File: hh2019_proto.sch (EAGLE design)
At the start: 145 parts, among them IC1 CP210X_USB_UART, IC2 AP2114H, IC4 TP4056, J1 PJ-313D, Q1 MMBT2222A, Q3 MMBT2222A, Q4 MMBT2222A, Q5 SI1304 BDL, T1 MOSFET-PCHANNEL, T2 MOSFET-PCHANNEL, U1 MPR121QR2, U2 ESP32-WROVER-I, U3 PCM5102A, X4 JST-PH3

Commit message: All but the last handful passives placed and routed
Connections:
- net N$8 renamed RST
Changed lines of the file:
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@@
 </segment>
 </net>
-<net name="N$8" class="0">
+<net name="RST" class="0">
 <segment>
 <pinref part="IC1" gate="G$1" pin="!RST"/>

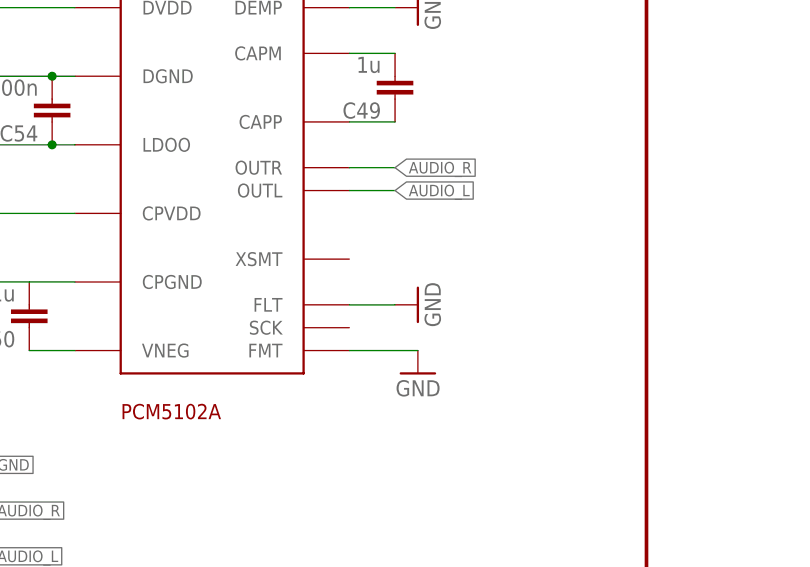
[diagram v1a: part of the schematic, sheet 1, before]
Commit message: Added missing DAC connections. Fixes #1
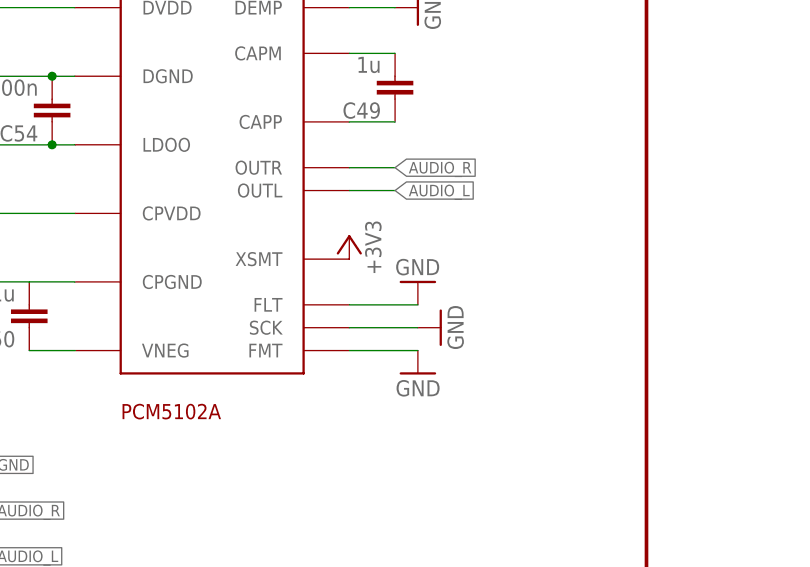
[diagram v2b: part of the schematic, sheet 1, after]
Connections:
- new net +3V3: U3.XSMT
- net GND: now also U3.SCK
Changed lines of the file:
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@@
 <part name="GND18" library="supply1" deviceset="GND" device=""/>
 <part name="GND55" library="supply1" deviceset="GND" device=""/>
+<part name="GND56" library="supply1" deviceset="GND" device=""/>
+<part name="+2V7" library="supply1" deviceset="+3V3" device=""/>
 </parts>
 <sheets>
@@
 <attribute name="VALUE" x="205.74" y="116.84" size="1.778" layer="96" rot="MR270"/>
 </instance>
-<instance part="GND3" gate="1" x="203.2" y="81.28" smashed="yes" rot="MR270">
-<attribute name="VALUE" x="205.74" y="83.82" size="1.778" layer="96" rot="MR270"/>
+<instance part="GND3" gate="1" x="203.2" y="83.82" smashed="yes" rot="MR180">
+<attribute name="VALUE" x="200.66" y="86.36" size="1.778" layer="96" rot="MR180"/>
 </instance>
 <instance part="GND17" gate="1" x="203.2" y="73.66" smashed="yes" rot="MR0">
@@
 <instance part="GND55" gate="1" x="144.78" y="104.14" smashed="yes" rot="MR0">
 <attribute name="VALUE" x="147.32" y="101.6" size="1.778" layer="96" rot="MR0"/>
+</instance>
+<instance part="GND56" gate="1" x="205.74" y="78.74" smashed="yes" rot="MR270">
+<attribute name="VALUE" x="208.28" y="81.28" size="1.778" layer="96" rot="MR270"/>
+</instance>
+<instance part="+2V7" gate="G$1" x="195.58" y="88.9" smashed="yes">
+<attribute name="VALUE" x="199.136" y="84.582" size="1.778" layer="96" rot="R90"/>
 </instance>
 </instances>
@@
 <segment>
 <pinref part="U3" gate="G$1" pin="FLT"/>
-<wire x1="195.58" y1="81.28" x2="200.66" y2="81.28" width="0.1524" layer="91"/>
+<wire x1="195.58" y1="81.28" x2="203.2" y2="81.28" width="0.1524" layer="91"/>
 <pinref part="GND3" gate="1" pin="GND"/>
 </segment>
@@
 <pinref part="C54" gate="G$1" pin="2"/>
 <pinref part="GND55" gate="1" pin="GND"/>
+</segment>
+<segment>
+<pinref part="U3" gate="G$1" pin="SCK"/>
+<pinref part="GND56" gate="1" pin="GND"/>
+<wire x1="203.2" y1="78.74" x2="195.58" y2="78.74" width="0.1524" layer="91"/>
 </segment>
 </net>
@@
 </segment>
 </net>
+<net name="+3V3" class="0">
+<segment>
+<pinref part="U3" gate="G$1" pin="XSMT"/>
+<pinref part="+2V7" gate="G$1" pin="+3V3"/>
+</segment>
+</net>

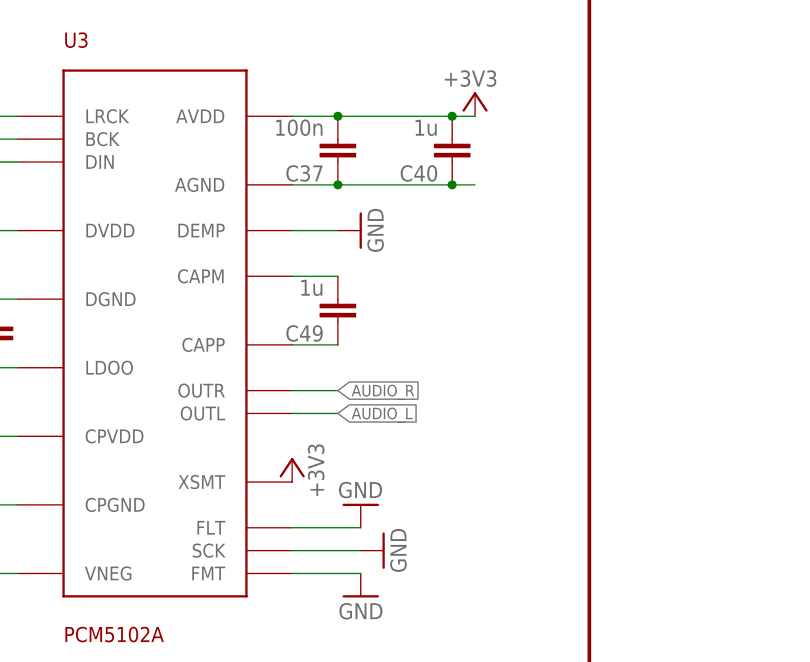
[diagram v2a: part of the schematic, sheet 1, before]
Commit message: Fixed floating DAC pins being unconnected
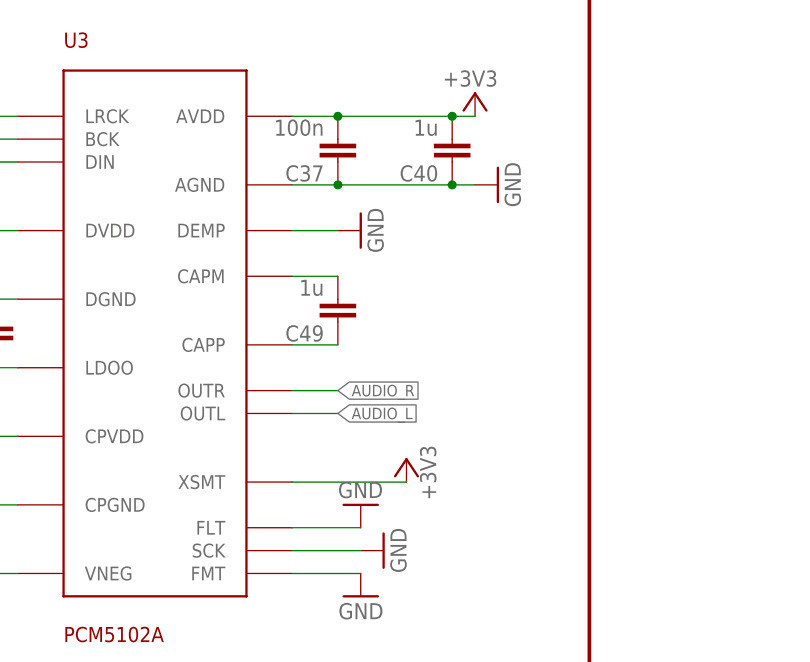
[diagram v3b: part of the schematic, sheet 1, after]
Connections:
- removed net +3V3: U3.XSMT
- removed net DEMP: U3.DEMP
- net 3V3: now also U3.XSMT
- net GND: now also U3.DEMP
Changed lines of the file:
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@@
 <part name="GND18" library="supply1" deviceset="GND" device=""/>
 <part name="GND55" library="supply1" deviceset="GND" device=""/>
+<part name="GND" library="supply1" deviceset="GND" device=""/>
 <part name="GND56" library="supply1" deviceset="GND" device=""/>
 <part name="+2V7" library="supply1" deviceset="+3V3" device=""/>
@@
 <attribute name="VALUE" x="147.32" y="101.6" size="1.778" layer="96" rot="MR0"/>
 </instance>
-<instance part="GND56" gate="1" x="205.74" y="78.74" smashed="yes" rot="MR270">
+<instance part="GND" gate="1" x="205.74" y="78.74" smashed="yes" rot="MR270">
 <attribute name="VALUE" x="208.28" y="81.28" size="1.778" layer="96" rot="MR270"/>
 </instance>
-<instance part="+2V7" gate="G$1" x="195.58" y="88.9" smashed="yes">
-<attribute name="VALUE" x="199.136" y="84.582" size="1.778" layer="96" rot="R90"/>
+<instance part="GND56" gate="1" x="218.44" y="119.38" smashed="yes" rot="MR270">
+<attribute name="VALUE" x="220.98" y="121.92" size="1.778" layer="96" rot="MR270"/>
+</instance>
+<instance part="+2V7" gate="G$1" x="208.28" y="88.9" smashed="yes">
+<attribute name="VALUE" x="211.582" y="84.328" size="1.778" layer="96" rot="R90"/>
 </instance>
 </instances>
@@
 <pinref part="C40" gate="G$1" pin="1"/>
 <junction x="213.36" y="119.38"/>
+<pinref part="GND56" gate="1" pin="GND"/>
 </segment>
 <segment>
@@
 <segment>
 <pinref part="U3" gate="G$1" pin="SCK"/>
-<pinref part="GND56" gate="1" pin="GND"/>
+<pinref part="GND" gate="1" pin="GND"/>
 <wire x1="203.2" y1="78.74" x2="195.58" y2="78.74" width="0.1524" layer="91"/>
+</segment>
+<segment>
+<pinref part="U3" gate="G$1" pin="DEMP"/>
+<wire x1="195.58" y1="114.3" x2="200.66" y2="114.3" width="0.1524" layer="91"/>
+<pinref part="GND2" gate="1" pin="GND"/>
 </segment>
 </net>
@@
 <pinref part="+2V6" gate="G$1" pin="+3V3"/>
 </segment>
+<segment>
+<pinref part="U3" gate="G$1" pin="XSMT"/>
+<pinref part="+2V7" gate="G$1" pin="+3V3"/>
+<wire x1="195.58" y1="86.36" x2="208.28" y2="86.36" width="0.1524" layer="91"/>
+</segment>
 </net>
 <net name="GDR" class="0">
@@
 </segment>
 </net>
-<net name="DEMP" class="2">
-<segment>
-<pinref part="U3" gate="G$1" pin="DEMP"/>
-<wire x1="195.58" y1="114.3" x2="200.66" y2="114.3" width="0.1524" layer="91"/>
-<pinref part="GND2" gate="1" pin="GND"/>
-</segment>
-</net>
-<net name="+3V3" class="0">
-<segment>
-<pinref part="U3" gate="G$1" pin="XSMT"/>
-<pinref part="+2V7" gate="G$1" pin="+3V3"/>
-</segment>
-</net>

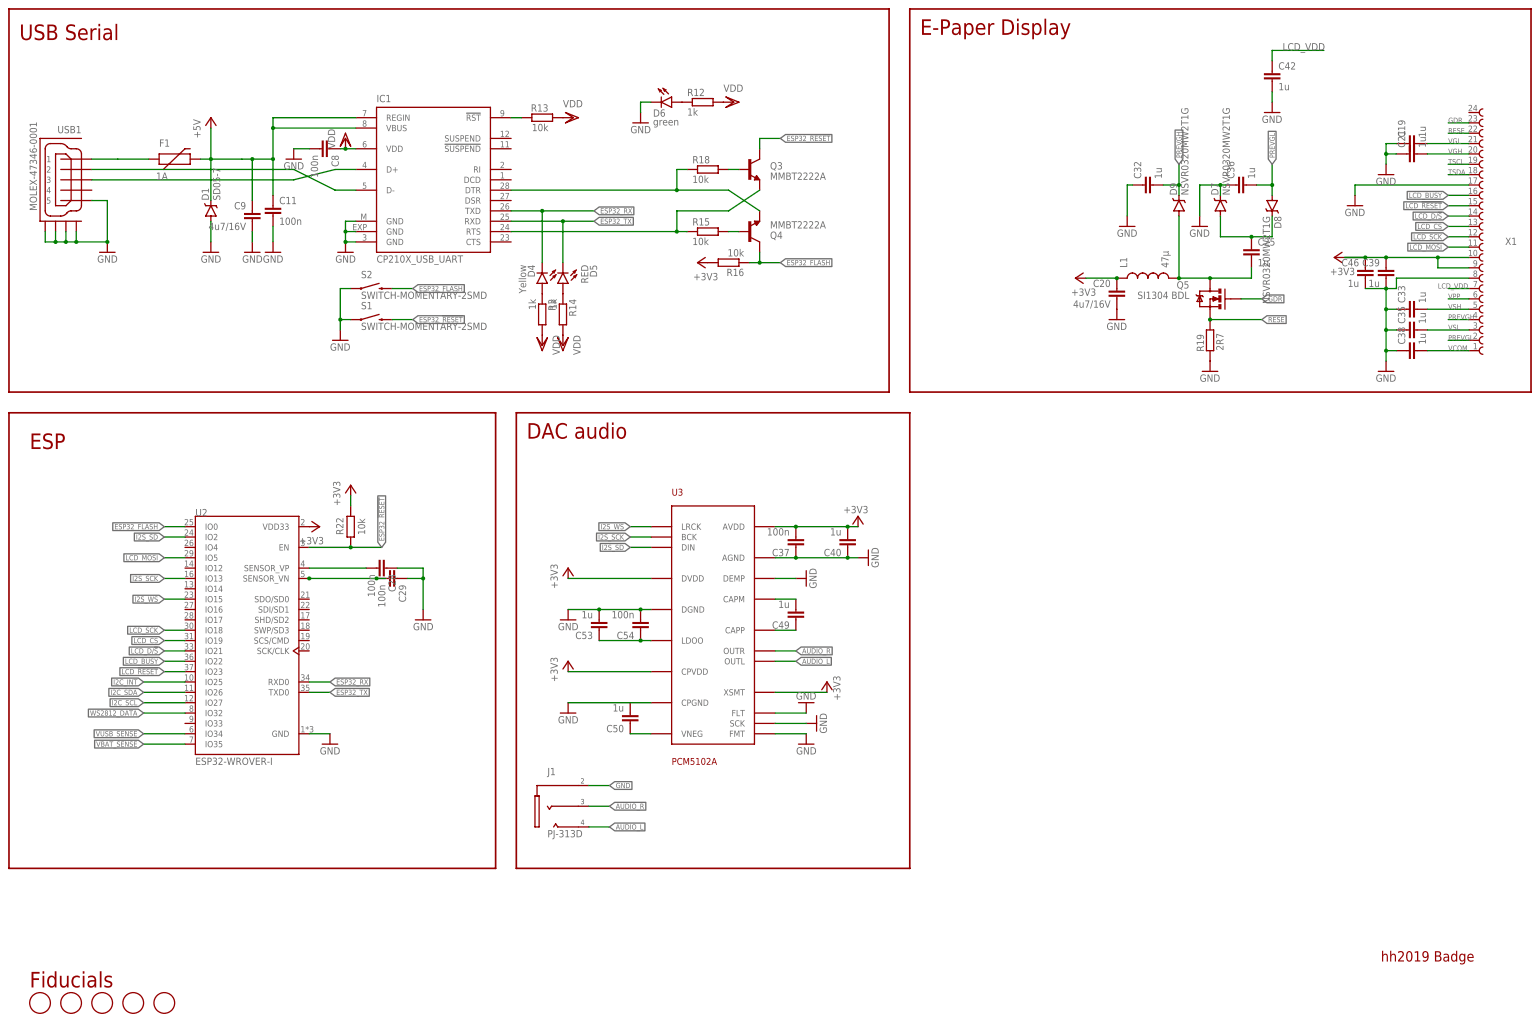
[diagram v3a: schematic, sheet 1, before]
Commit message: Finished PCB design. Added Shitty AddOn, IR, buzzer
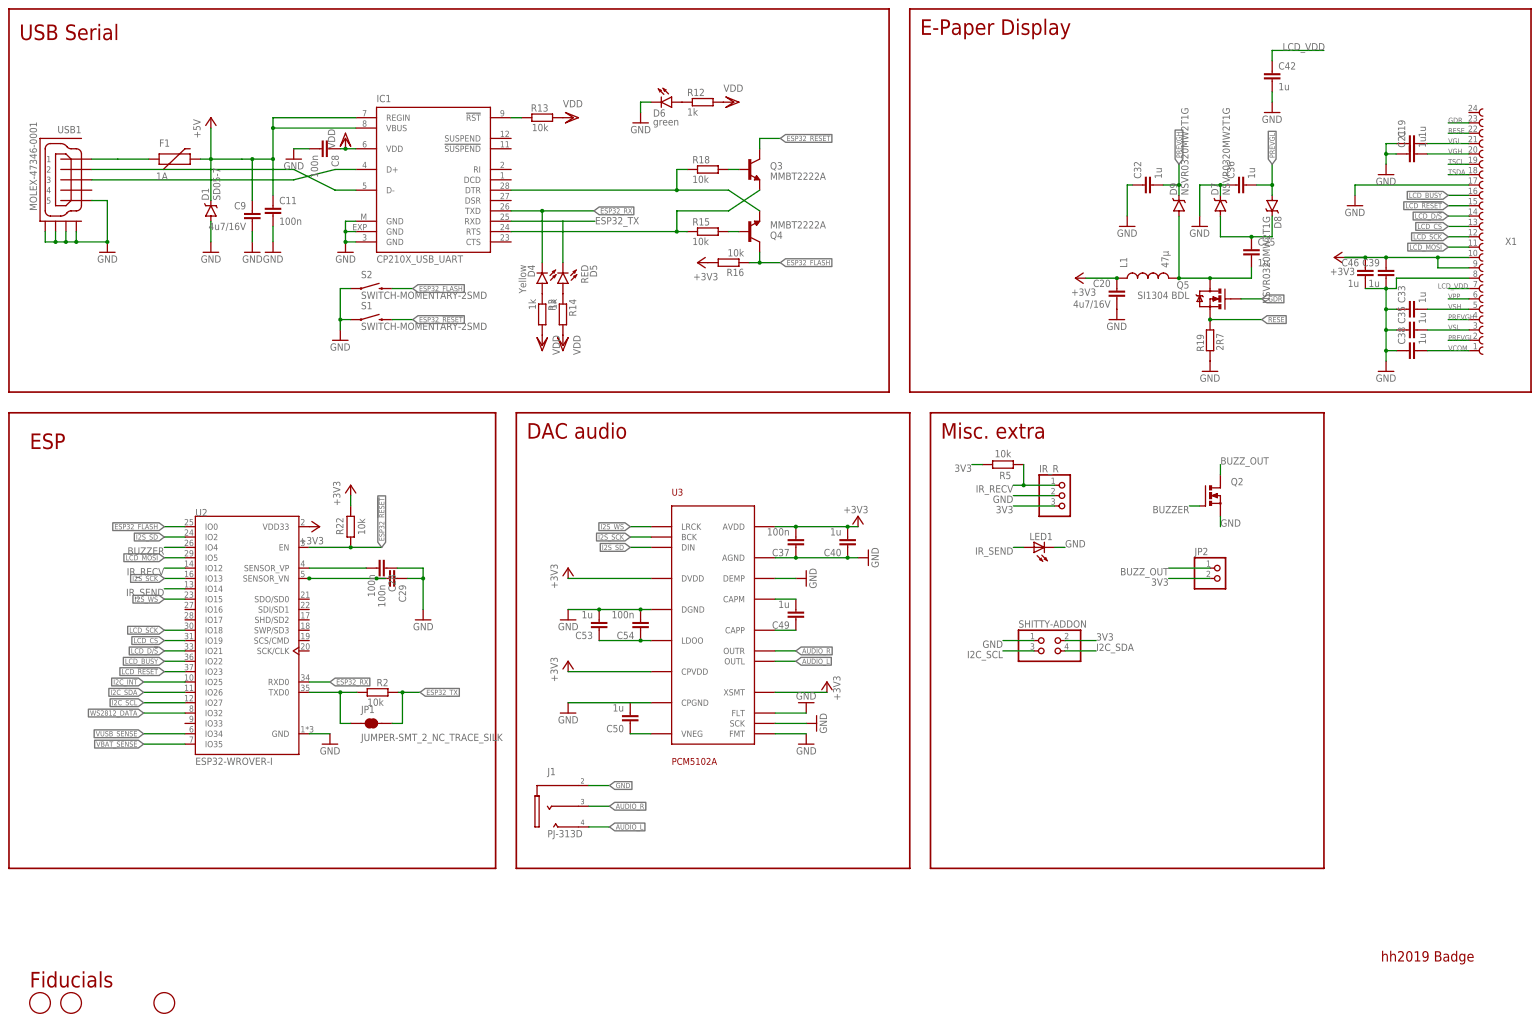
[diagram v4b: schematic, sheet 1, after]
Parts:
- removed $$U$1, $$U$2, $$U$3, $$U$4, $$U$5, $$U$6, $$U$7, $$U$8, $$U$9, U$10, U$11, U$12, U$13, U$14, U$15, U$16, U$17, U$18, U$19, U$2, U$20, U$21, U$22, U$23, U$3, U$4, U$5, U$6: VIA, badge:VIA
- removed FD2, FD3: FIDUCIAL, adafruit:FIDUCIAL
- added IR_R: (no value), pinhead:PINHD-1X3
- added JP1: JUMPER-SMT_2_NC_TRACE_SILK, SparkFun-Jumpers:JUMPER-SMT_2_NC_TRACE_SILK
- added JP2: (no value), pinhead:PINHD-1X2
- added LED1: (no value), led:LED5MM
- added Q2: (no value), transistor-power:N-MOSFET-SO8S
- added R2, R5: 10k, hh2019_proto:R0603-DASHES
- added SHITTY-ADDON: (no value), pinhead:PINHD-2X2
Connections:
- new net BUZZER: Q2.G, U2.IO4
- new net BUZZ_OUT: JP2.1, Q2.D
- new net ESP32_TX_PRE: JP1.1, R2.2, U2.TXD0
- new net IR_RECV: IR_R.1, R5.2, U2.IO12
- new net IR_SEND: LED1.A, U2.IO14
- net 3V3: now also IR_R.3, JP2.2, R5.1, SHITTY-ADDON.2
- net ESP32_TX: now also JP1.2, R2.1; no longer U2.TXD0
- net GND: now also IR_R.2, LED1.C, Q2.S, SHITTY-ADDON.1; no longer $$U$1.P$1, $$U$2.P$1, $$U$3.P$1, $$U$4.P$1, $$U$5.P$1, $$U$6.P$1, $$U$7.P$1, $$U$8.P$1, $$U$9.P$1, U$10.P$1, U$11.P$1, U$12.P$1, U$13.P$1, U$14.P$1, U$15.P$1, U$16.P$1, U$17.P$1, U$18.P$1, U$19.P$1, U$2.P$1, U$20.P$1, U$21.P$1, U$22.P$1, U$23.P$1, U$3.P$1, U$4.P$1, U$5.P$1, U$6.P$1
- net I2C_SCL: now also SHITTY-ADDON.3
- net I2C_SDA: now also SHITTY-ADDON.4
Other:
- note added: "Misc. extra"
- note removed: "Special Vias with thermals (hack)"

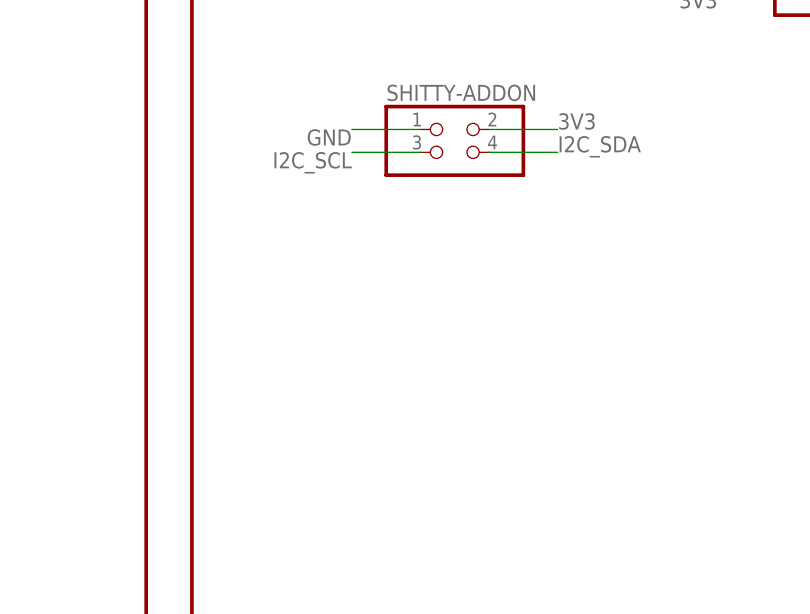
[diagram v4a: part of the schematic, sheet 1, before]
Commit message: Added Renze's superfluous Grove connector
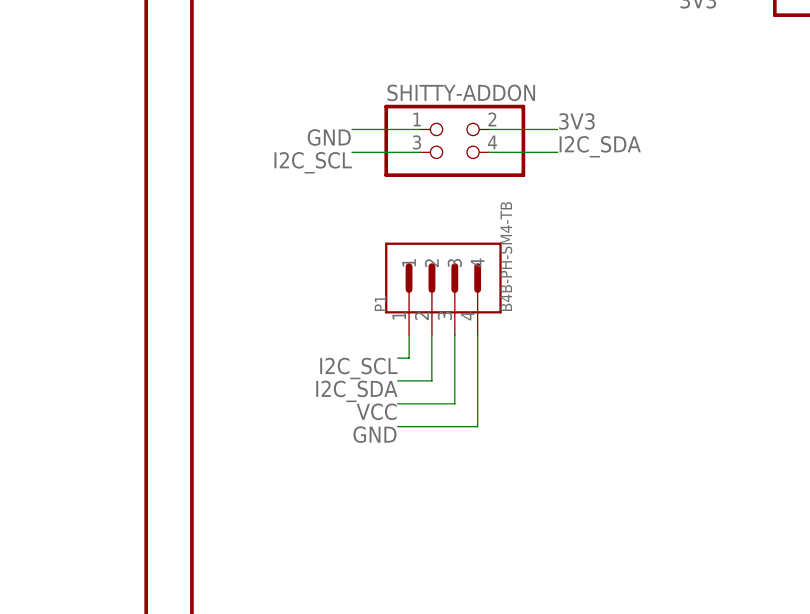
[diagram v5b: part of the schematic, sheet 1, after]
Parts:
- added P1: B4B-PH-SM4-TB, B4B-PH-SM4-TB:B4B-PH-SM4-TB
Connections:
- net GND: now also P1.4
- net I2C_SCL: now also P1.1
- net I2C_SDA: now also P1.2
- net VCC: now also P1.3
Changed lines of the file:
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@@
 <part name="JP2" library="pinhead" library_urn="urn:adsk.eagle:library:325" deviceset="PINHD-1X2" device="" package3d_urn="urn:adsk.eagle:package:22435/2"/>
 <part name="SHITTY-ADDON" library="pinhead" library_urn="urn:adsk.eagle:library:325" deviceset="PINHD-2X2" device="" package3d_urn="urn:adsk.eagle:package:22455/2"/>
+<part name="P1" library="B4B-PH-SM4-TB" deviceset="B4B-PH-SM4-TB" device=""/>
 </parts>
 <sheets>
@@
 <attribute name="VALUE" x="255.27" y="91.44" size="1.778" layer="96"/>
 </instance>
+<instance part="P1" gate="G$1" x="261.62" y="81.28" smashed="yes" rot="R90">
+<attribute name="NAME" x="255.26641875" y="78.73856875" size="1.27071875" layer="95" rot="R90"/>
+<attribute name="VALUE" x="269.249040625" y="78.736990625" size="1.271509375" layer="96" rot="R90"/>
+</instance>
 </instances>
 <busses>
@@
 <wire x1="259.08" y1="99.06" x2="251.46" y2="99.06" width="0.1524" layer="91"/>
 <label x="251.46" y="99.06" size="1.778" layer="95" rot="R180"/>
+</segment>
+<segment>
+<pinref part="P1" gate="G$1" pin="4"/>
+<wire x1="265.43" y1="76.2" x2="265.43" y2="66.04" width="0.1524" layer="91"/>
+<wire x1="265.43" y1="66.04" x2="256.54" y2="66.04" width="0.1524" layer="91"/>
+<label x="256.54" y="66.04" size="1.778" layer="95" rot="R180"/>
 </segment>
 </net>
@@
 <label x="274.32" y="96.52" size="1.778" layer="95"/>
 </segment>
+<segment>
+<pinref part="P1" gate="G$1" pin="2"/>
+<wire x1="260.35" y1="76.2" x2="260.35" y2="71.12" width="0.1524" layer="91"/>
+<wire x1="260.35" y1="71.12" x2="256.54" y2="71.12" width="0.1524" layer="91"/>
+<label x="256.54" y="71.12" size="1.778" layer="95" rot="R180"/>
+</segment>
 </net>
 <net name="I2C_SCL" class="0">
@@
 <wire x1="259.08" y1="96.52" x2="251.46" y2="96.52" width="0.1524" layer="91"/>
 <label x="251.46" y="96.52" size="1.778" layer="95" rot="R180"/>
+</segment>
+<segment>
+<pinref part="P1" gate="G$1" pin="1"/>
+<wire x1="257.81" y1="76.2" x2="257.81" y2="73.66" width="0.1524" layer="91"/>
+<wire x1="257.81" y1="73.66" x2="256.54" y2="73.66" width="0.1524" layer="91"/>
+<label x="256.54" y="73.66" size="1.778" layer="95" rot="R180"/>
 </segment>
 </net>
@@
 </segment>
 </net>
+<net name="VCC" class="1">
+<segment>
+<pinref part="P1" gate="G$1" pin="3"/>
+<wire x1="262.89" y1="76.2" x2="262.89" y2="68.58" width="0.1524" layer="91"/>
+<wire x1="262.89" y1="68.58" x2="256.54" y2="68.58" width="0.1524" layer="91"/>
+<label x="256.54" y="68.58" size="1.778" layer="95" rot="R180"/>
+</segment>
+</net>
